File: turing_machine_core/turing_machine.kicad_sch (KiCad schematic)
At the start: 13 parts, among them U1 74LS04, U10 74LS193, U11 AS6C1008, U12 74LS193, U13 74LS374, U2 74LS00, U3 AS6C1008, U4 74LS00, U5 74LS193, U6 74LS374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

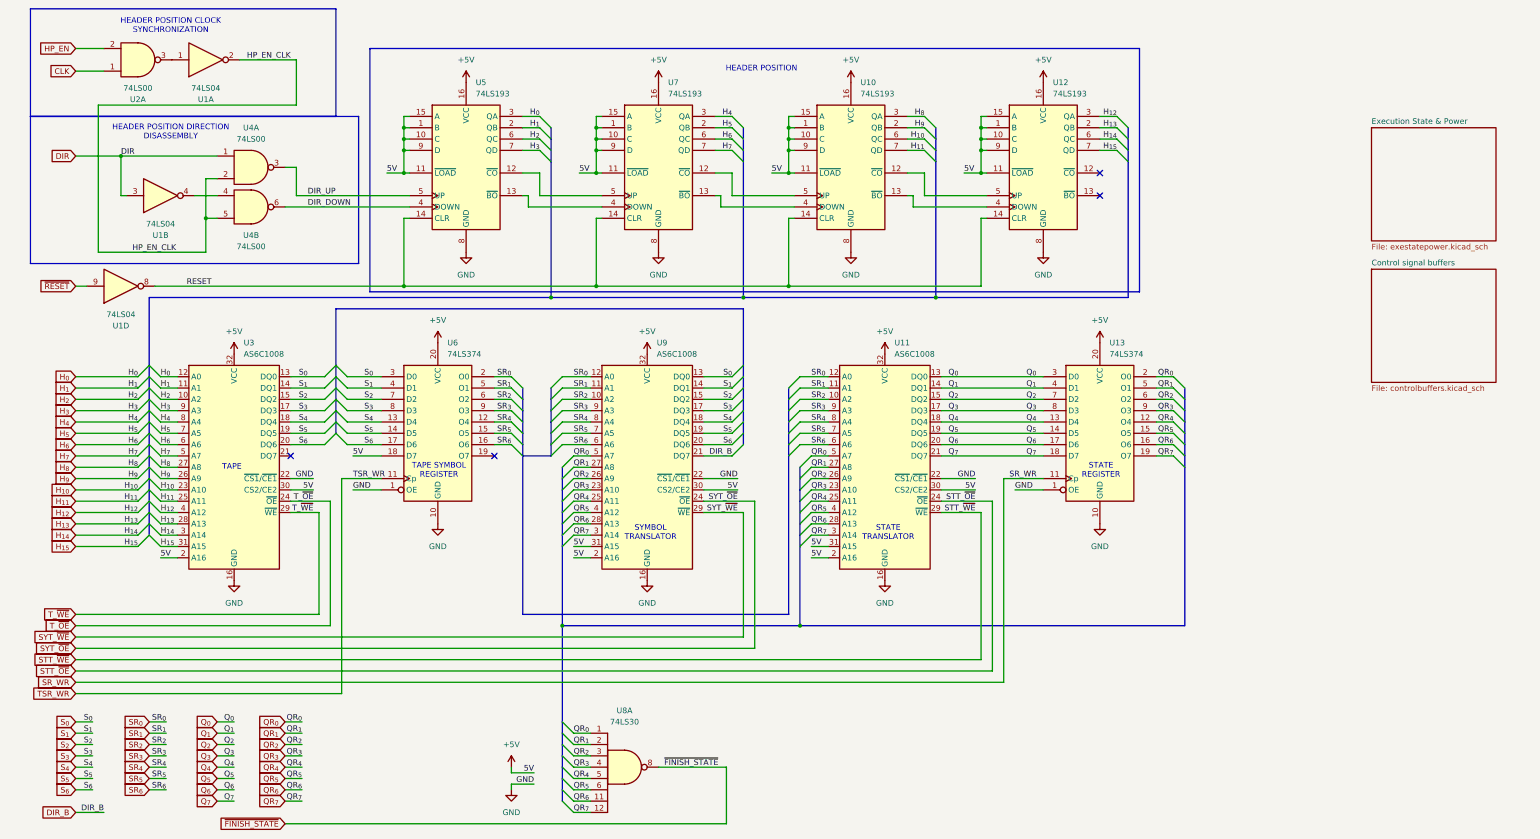
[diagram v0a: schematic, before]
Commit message: PCB layout planning and further documantation work
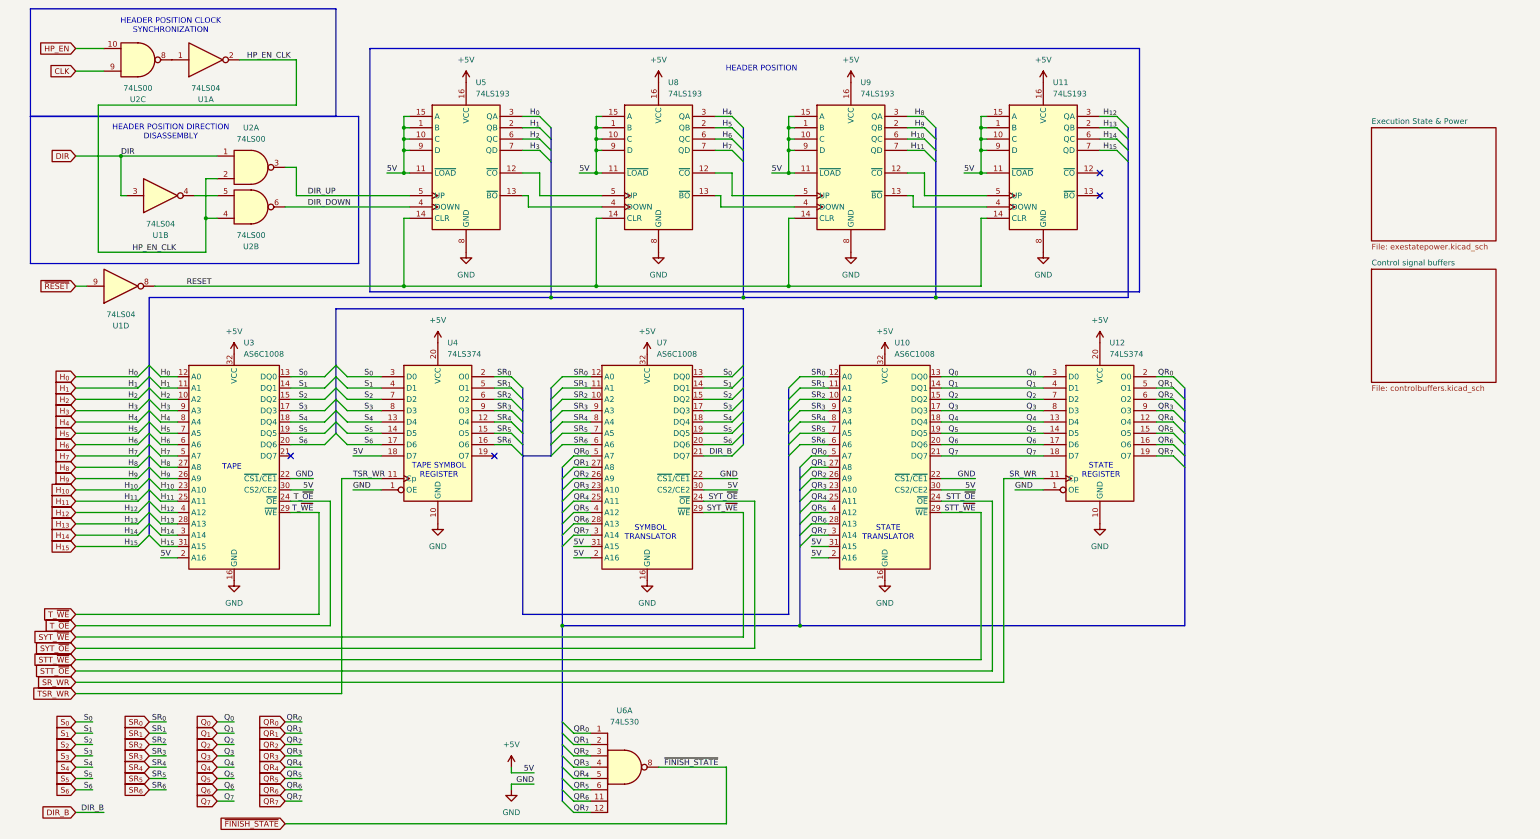
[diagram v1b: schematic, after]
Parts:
- removed U4: 74LS00, symbol 74xx:74LS00
- added unit 3 of U2
- added unit 2 of U2
- U1: footprint (none) -> Package_DIP:DIP-14_W7.62mm
- U10: renamed from U11; footprint Package_DIP:DIP-32_W15.24mm -> Package_DIP:DIP-32_W15.24mm_Socket
- U3: footprint Package_DIP:DIP-32_W15.24mm -> Package_DIP:DIP-32_W15.24mm_Socket
- U6: renamed from U8; footprint (none) -> Package_DIP:DIP-14_W7.62mm
- U7: renamed from U9; footprint Package_DIP:DIP-32_W15.24mm -> Package_DIP:DIP-32_W15.24mm_Socket
- renumbered U12 to U11, U13 to U12, U6 to U4, U7 to U8, U10 to U9
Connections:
- net CLK: now also U2.9; no longer U2.1
- net DIR: now also U2.1
- net DIR_DOWN: now also U2.6
- net DIR_UP: now also U2.3
- net HP_EN: now also U2.10; no longer U2.2
- net HP_EN_CLK: now also U2.2, U2.4
- net at U1.4: now also U2.5
- net at U1.1: now also U2.8; no longer U2.3

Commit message: small cosmetic PCB changes
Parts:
- U10, U3, U7: footprint Package_DIP:DIP-32_W15.24mm_Socket -> Package_DIP:DIP-32_W15.24mm
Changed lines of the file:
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@@
 			)
 		)
-		(property "Footprint" "Package_DIP:DIP-32_W15.24mm_Socket"
+		(property "Footprint" "Package_DIP:DIP-32_W15.24mm"
 			(at 60.96 115.57 0)
 			(effects
@@
 			)
 		)
-		(property "Footprint" "Package_DIP:DIP-32_W15.24mm_Socket"
+		(property "Footprint" "Package_DIP:DIP-32_W15.24mm"
 			(at 153.67 115.57 0)
 			(effects
@@
 			)
 		)
-		(property "Footprint" "Package_DIP:DIP-32_W15.24mm_Socket"
+		(property "Footprint" "Package_DIP:DIP-32_W15.24mm"
 			(at 207.01 115.57 0)
 			(effects
